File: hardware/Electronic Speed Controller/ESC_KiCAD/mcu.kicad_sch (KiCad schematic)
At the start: 24 parts, among them J1 XT60, J3 2x2-2.54MM, J4 S2B-PH-K-S, J5 S2B-PH-K-S, U1 R-78CK5.0-0.5, U2 TLV75533PDBVR, U6 SN65HVD232D, U7 STM32G431KBT6

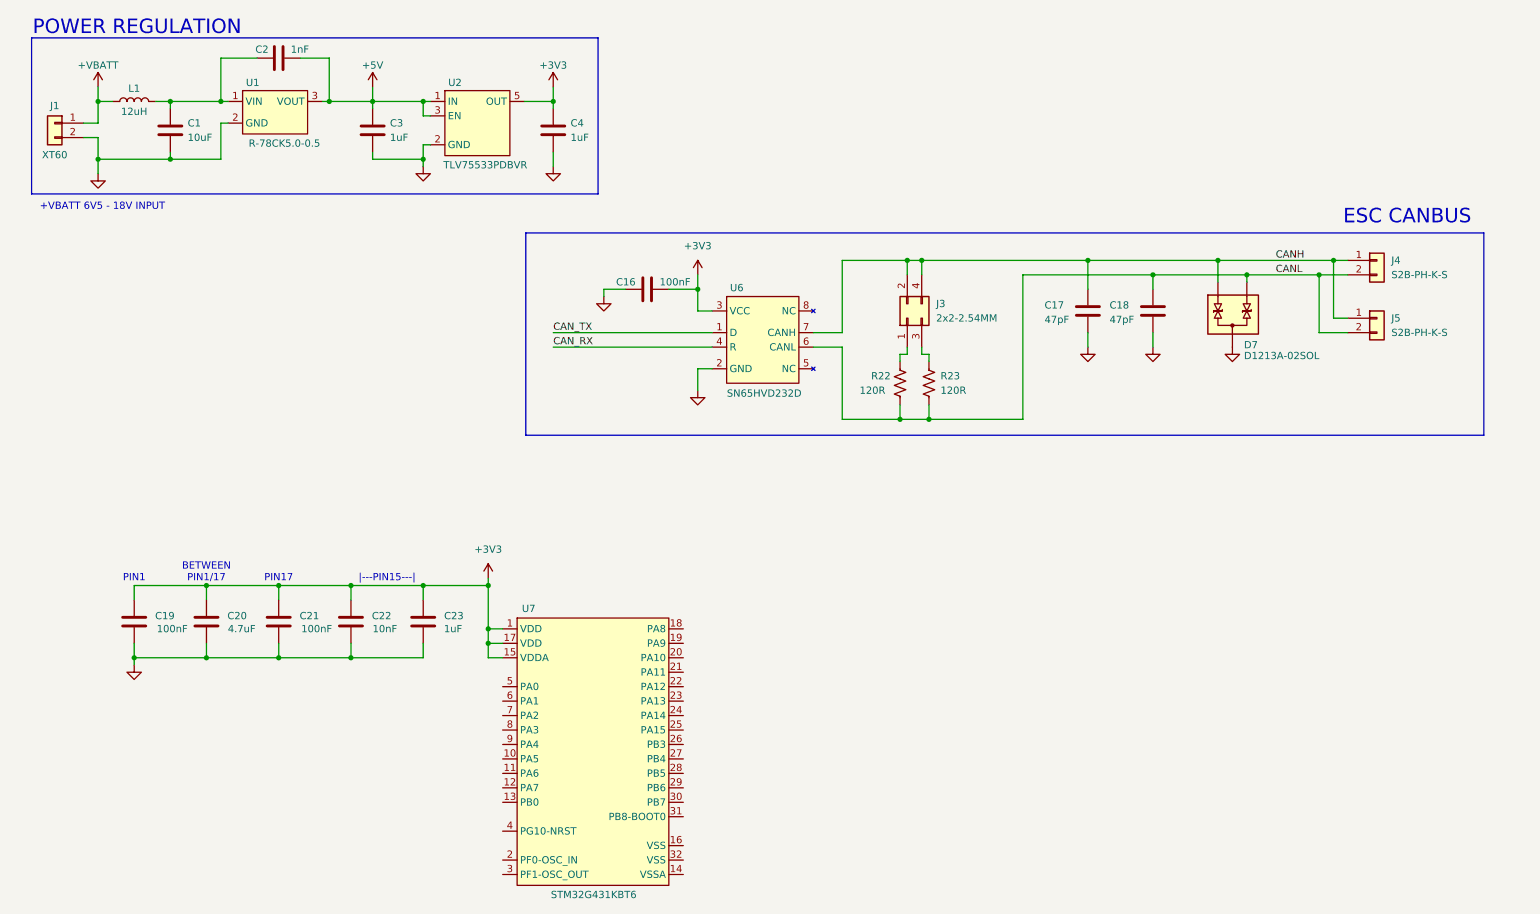
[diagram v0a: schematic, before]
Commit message: esc sensing circuitry
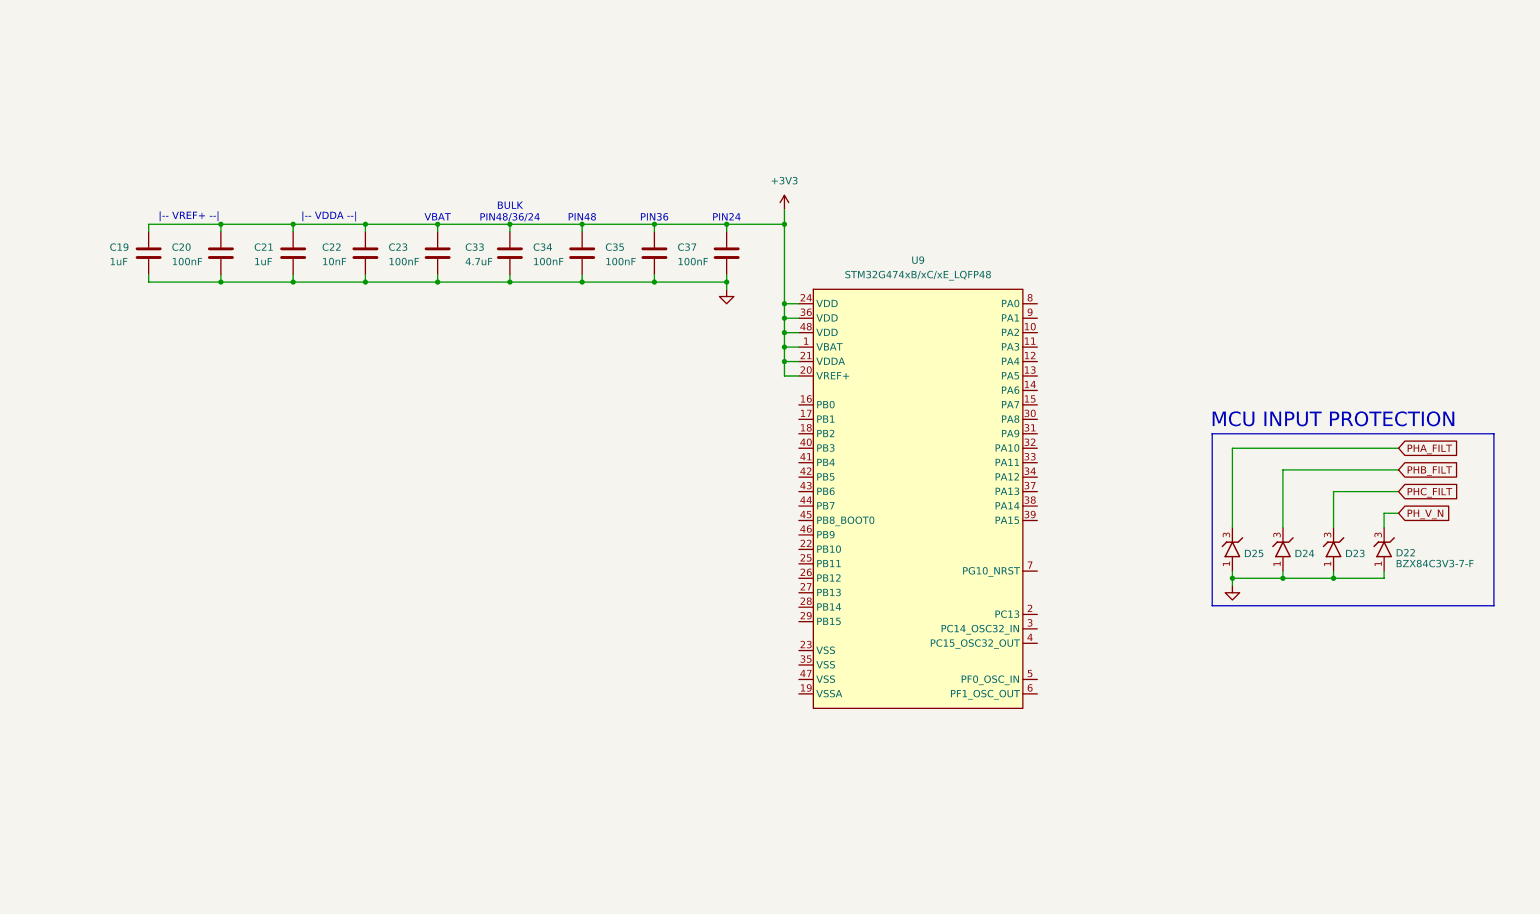
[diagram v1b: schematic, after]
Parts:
- removed C1: 10uF, symbol Device:C
- removed C16: 100nF, Capacitors:CAP_0402_1005Metric, symbol Device:C
- removed C17, C18: 47pF, Capacitors:CAP_0402_1005Metric, symbol Device:C
- removed C2: 1nF, symbol Device:C
- removed C3, C4: 1uF, symbol Device:C
- removed D7: D1213A-02SOL, Diodes:DiodesINC_SOT23-3, symbol Diodes:TVS_BIDIRECTIONAL_2CH
- removed J1: XT60, Connectors:CONN_MALE_TH_XT60, symbol Connector_Generic:Conn_01x02
- removed J3: 2x2-2.54MM, Connectors:CONN_MALE_TH_2.54MM_2x2, symbol Connector_Generic:Conn_02x02_Odd_Even
- removed J4, J5: S2B-PH-K-S, Connectors:CONN_JST_S2B-PH-K-S, symbol Connector_Generic:Conn_01x02
- removed L1: 12uH, Inductors:Abracon_ASPI-6045S, symbol Device:L
- removed R22, R23: 120R, Resistors:RES_0603_1608Metric, symbol Device:R_US
- removed U1: R-78CK5.0-0.5, ICs:RECOM_SIP-3, symbol ICs:R-78CKxx-0.5
- removed U2: TLV75533PDBVR, ICs:TI_SOT23-5, symbol ICs:TLV755P-DBV
- removed U6: SN65HVD232D, ICs:TI_SOIC-8, symbol ICs:SN65HVD232D
- removed U7: STM32G431KBT6, ICs:STM_LQFP32, symbol ICs:STM32G431x6/x8/xB_LQFP32
- added C33: 4.7uF, Capacitors:CAP_0402_1005Metric, symbol Device:C
- added C34, C35, C37: 100nF, Capacitors:CAP_0402_1005Metric, symbol Device:C
- added D22, D23, D24, D25: BZX84C3V3-7-F, Diodes:DiodesINC_SOT23-3, symbol Diodes:ZENER
- added U9: STM32G474xB/xC/xE_LQFP48, ICs:STM_LQFP48, symbol ICs:STM32G474xB/xC/xE_LQFP48
- C19, C21: value 100nF -> 1uF; JLCPCB Part# C77020 -> C77009
- C20: value 4.7uF -> 100nF
- C22: JLCPCB Part# C77020 -> C162190
- C23: value 1uF -> 100nF
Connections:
- net +3V3: now also C19.1, C20.1, C21.1, C22.1, C23.1, C33.1, C34.1, C35.1, C37.1, U9.1 (VBAT), U9.20 (VREF+), U9.21 (VDDA), U9.24 (VDD), U9.36 (VDD), U9.48 (VDD); no longer C19.2, C20.2, C21.2, C22.2, C23.2
- net GND: now also C19.2, C20.2, C21.2, C22.2, C23.2, C33.2, C34.2, C35.2, C37.2, D22.1 (A), D23.1 (A), D24.1 (A), D25.1 (A); no longer C19.1, C20.1, C21.1, C22.1, C23.1
- new net PHA_FILT: D25.3 (K)
- new net PHB_FILT: D24.3 (K)
- new net PHC_FILT: D23.3 (K)
- new net PH_V_N: D22.3 (K)
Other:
- note added: "BULK PIN48/36/24"
- note added: "MCU INPUT PROTECTION"
- note added: "PIN24"
- note added: "PIN36"
- note added: "PIN48"
- note added: "VBAT"
- note added: "|-- VDDA --|"
- note added: "|-- VREF+ --|"
- note removed: "+VBATT 6V5 - 18V INPUT"
- note removed: "BETWEEN PIN1/17"
- note removed: "ESC CANBUS"
- note removed: "PIN1"
- note removed: "PIN17"
- note removed: "POWER REGULATION"
- note removed: "|---PIN15---|"
- title: (none) -> MICROCONTROLLER

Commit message: finish ESC hardware RevA, CC2500 driver working
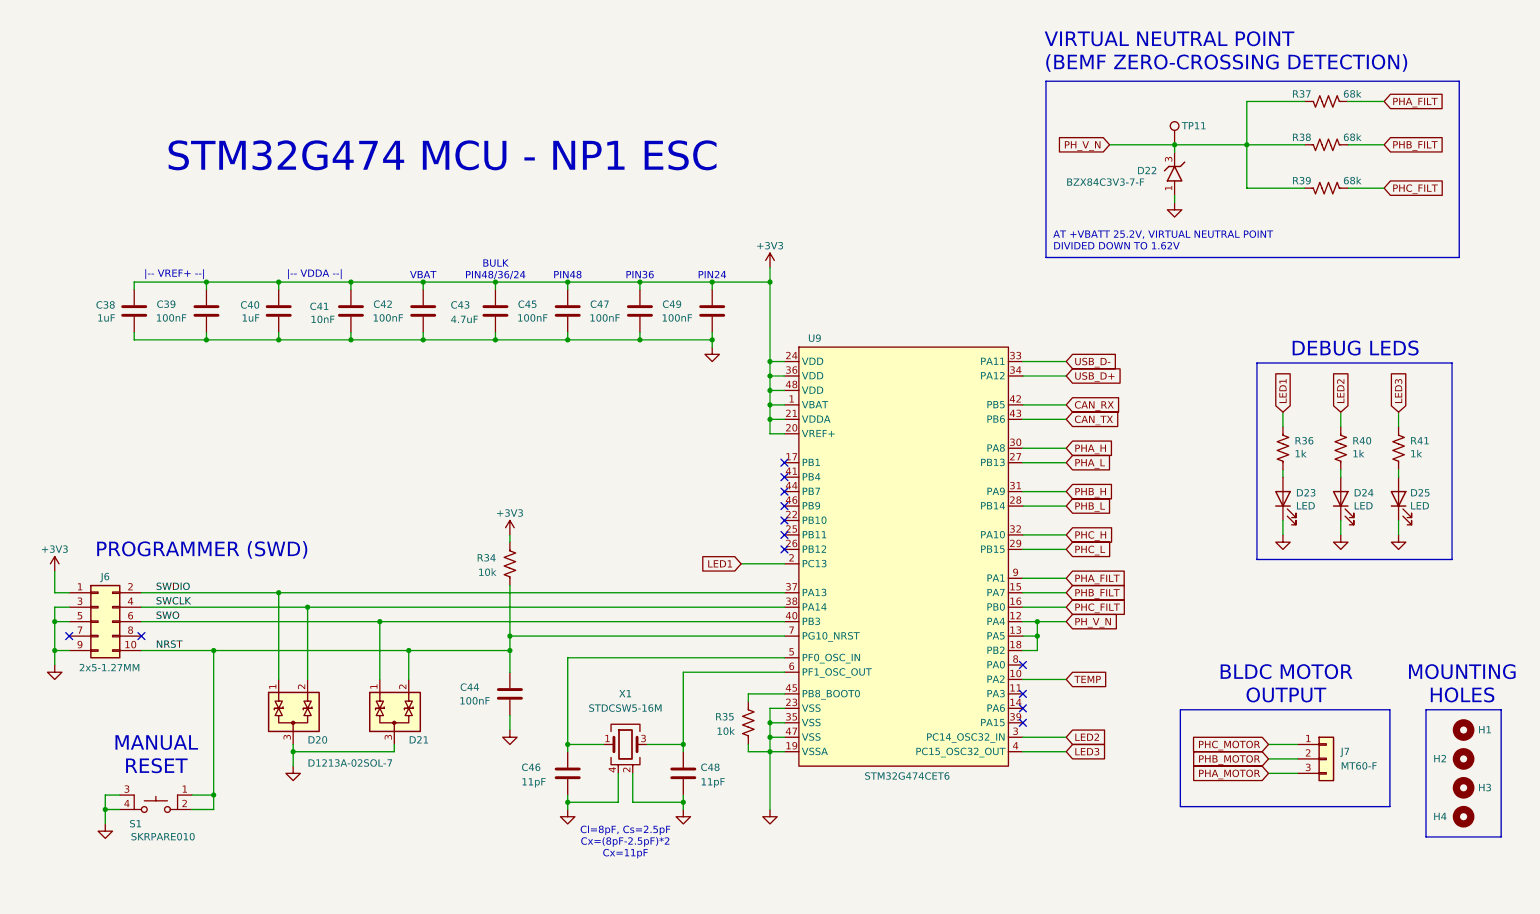
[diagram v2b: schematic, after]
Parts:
- removed C19, C21: 1uF, Capacitors:CAP_0402_1005Metric, symbol Device:C
- removed C20, C23, C34, C35, C37: 100nF, Capacitors:CAP_0402_1005Metric, symbol Device:C
- removed C22: 10nF, Capacitors:CAP_0402_1005Metric, symbol Device:C
- removed D23, D24, D25: BZX84C3V3-7-F, Diodes:DiodesINC_SOT23-3, symbol Diodes:ZENER
- added C38, C40: 1uF, Capacitors:CAP_0805_2012Metric, symbol Device:C
- added C39, C42, C44, C45, C47, C49: 100nF, Capacitors:CAP_0603_1608Metric, symbol Device:C
- added C41: 10nF, Capacitors:CAP_0603_1608Metric, symbol Device:C
- added C46, C48: 11pF, Capacitors:CAP_0402_1005Metric, symbol Device:C
- added D20, D21: D1213A-02SOL-7, Diodes:DiodesINC_SOT23-3, symbol Diodes:TVS_BIDIRECTIONAL_2CH
- added D23, D24, D25: LED, Diodes:LED_0603_1608Metric, symbol Device:LED
- added H1, H2, H3, H4: MountingHole, MountingHole:MountingHole_3.2mm_M3_ISO7380_Pad, symbol Mechanical:MountingHole
- added J6: 2x5-1.27MM, Connectors:CONN_MALE_SMT_1.27MM_2x5, symbol Connector_Generic:Conn_02x05_Odd_Even
- added J7: MT60-F, Connectors:CONN_MALE_TH_MT60, symbol Connector_Generic:Conn_01x03
- added R34, R35: 10k, Resistors:RES_0603_1608Metric, symbol Device:R_US
- added R36, R40, R41: 1k, Resistors:RES_0603_1608Metric, symbol Device:R_US
- added R37, R38, R39: 68k, Resistors:RES_0603_1608Metric, symbol Device:R_US
- added S1: SKRPARE010, Switches:TACT_SKRP, symbol Switches:TACT-SPST-4PIN
- added TP11: TestPoint, TestPoint:TestPoint_THTPad_D2.5mm_Drill1.2mm, symbol Connector:TestPoint
- added X1: STDCSW5-16M, CrystalsAndOscillators:NDK_NX2520SA, symbol CrystalsAndOscillators:NX2520SA
- C43: renamed from C33; footprint Capacitors:CAP_0402_1005Metric -> Capacitors:CAP_0805_2012Metric; JLCPCB Part # (none) -> C1779; JLCPCB Part# C77004 -> (none); Manufacturer (none) -> Samsung Electro-Mechanics; Manufacturer Part # (none) -> CL21A475KAQNNNE
- U9: value STM32G474xB/xC/xE_LQFP48 -> STM32G474CET6; JLCPCB Part # (none) -> C730125; Manufacturer (none) -> STMicroelectronics; Manufacturer Part # (none) -> STM32G474CET6
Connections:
- net +3V3: now also C38.2, C39.2, C40.2, C41.2, C42.2, C45.2, C47.2, C49.2, J6.1 (Pin_1), R34.1
- net GND: now also U9.19 (VSSA), U9.23 (VSS), U9.35 (VSS), U9.47 (VSS), C38.1, C39.1, C40.1, C41.1, C42.1, C44.1, C45.1, C46.2, C47.1, C48.2, C49.1, D20.3 (A), D21.3 (A), D23.1 (K), D24.1 (K), D25.1 (K), J6.3 (Pin_3), J6.5 (Pin_5), J6.9 (Pin_9), R35.2, S1.3, S1.4, X1.2, X1.4
- net PHA_FILT: now also U9.9 (PA1), R37.2
- net PHB_FILT: now also U9.15 (PA7), R38.2
- net PHC_FILT: now also U9.16 (PB0), R39.2
- net PH_V_N: now also U9.12 (PA4), U9.13 (PA5), U9.18 (PB2), R37.1, R38.1, R39.1, TP11.1
- net TEMP: now reaches U9.10 (PA2)
- net LED1: now reaches U9.2 (PC13)
- net LED1: now also R36.1
- net PHA_L: now reaches U9.27 (PB13)
- net PHB_L: now reaches U9.28 (PB14)
- net PHC_L: now reaches U9.29 (PB15)
- net LED2: now reaches U9.3 (PC14_OSC32_IN)
- net LED2: now also R40.1
- net PHA_H: now reaches U9.30 (PA8)
- net PHB_H: now reaches U9.31 (PA9)
- net PHC_H: now reaches U9.32 (PA10)
- net USB_D-: now reaches U9.33 (PA11)
- net USB_D+: now reaches U9.34 (PA12)
- net SWDIO: now reaches U9.37 (PA13)
- net SWDIO: now also D20.1 (K), J6.2 (Pin_2)
- net SWCLK: now reaches U9.38 (PA14)
- net SWCLK: now also D20.2 (K), J6.4 (Pin_4)
- net LED3: now reaches U9.4 (PC15_OSC32_OUT)
- net LED3: now also R41.1
- net SWO: now reaches U9.40 (PB3)
- net SWO: now also D21.1 (K), J6.6 (Pin_6)
- net CAN_RX: now reaches U9.42 (PB5)
- net CAN_TX: now reaches U9.43 (PB6)
- net at U9.45 (PB8_BOOT0): now also R35.1
- net at U9.5 (PF0_OSC_IN): now also C46.1, X1.1
- net at U9.6 (PF1_OSC_OUT): now also C48.1, X1.3
- net NRST: now reaches U9.7 (PG10_NRST)
- net NRST: now also C44.2, D21.2 (K), J6.10 (Pin_10), R34.2, S1.1, S1.2
- new net: D23.2 (A), R36.2
- new net: D24.2 (A), R40.2
- new net: D25.2 (A), R41.2
- new net PHA_MOTOR: J7.3 (Pin_3)
- new net PHB_MOTOR: J7.2 (Pin_2)
- new net PHC_MOTOR: J7.1 (Pin_1)
- no-connect marks 0 -> 13
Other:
- note added: "AT +VBATT 25.2V, VIRTUAL NEUTRAL POINT DIVIDED DOWN TO 1.62V"
- note added: "BLDC MOTOR OUTPUT"
- note added: "Cl=8pF, Cs=2.5pF Cx=(8pF-2.5pF)*2 Cx=11pF"
- note added: "DEBUG LEDS"
- note added: "MANUAL RESET"
- note added: "MOUNTING HOLES"
- note added: "PROGRAMMER (SWD)"
- note added: "STM32G474 MCU - NP1 ESC"
- note added: "VIRTUAL NEUTRAL POINT (BEMF ZERO-CROSSING DETECTION)"
- note removed: "MCU INPUT PROTECTION"
- moved on the sheet: C43
